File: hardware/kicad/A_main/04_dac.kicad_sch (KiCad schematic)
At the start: 34 parts, among them J30 SMA TX1, J31 SMA TX2, J32 SMA TX3, J33 SMA TX4, T10 ADT1-1WT+, T11 ADT1-1WT+, T12 ADT1-1WT+, T13 ADT1-1WT+, U10 LFE5U-25F-7BG256I, U30 AD9767ASTZ, U31 AD9767ASTZ

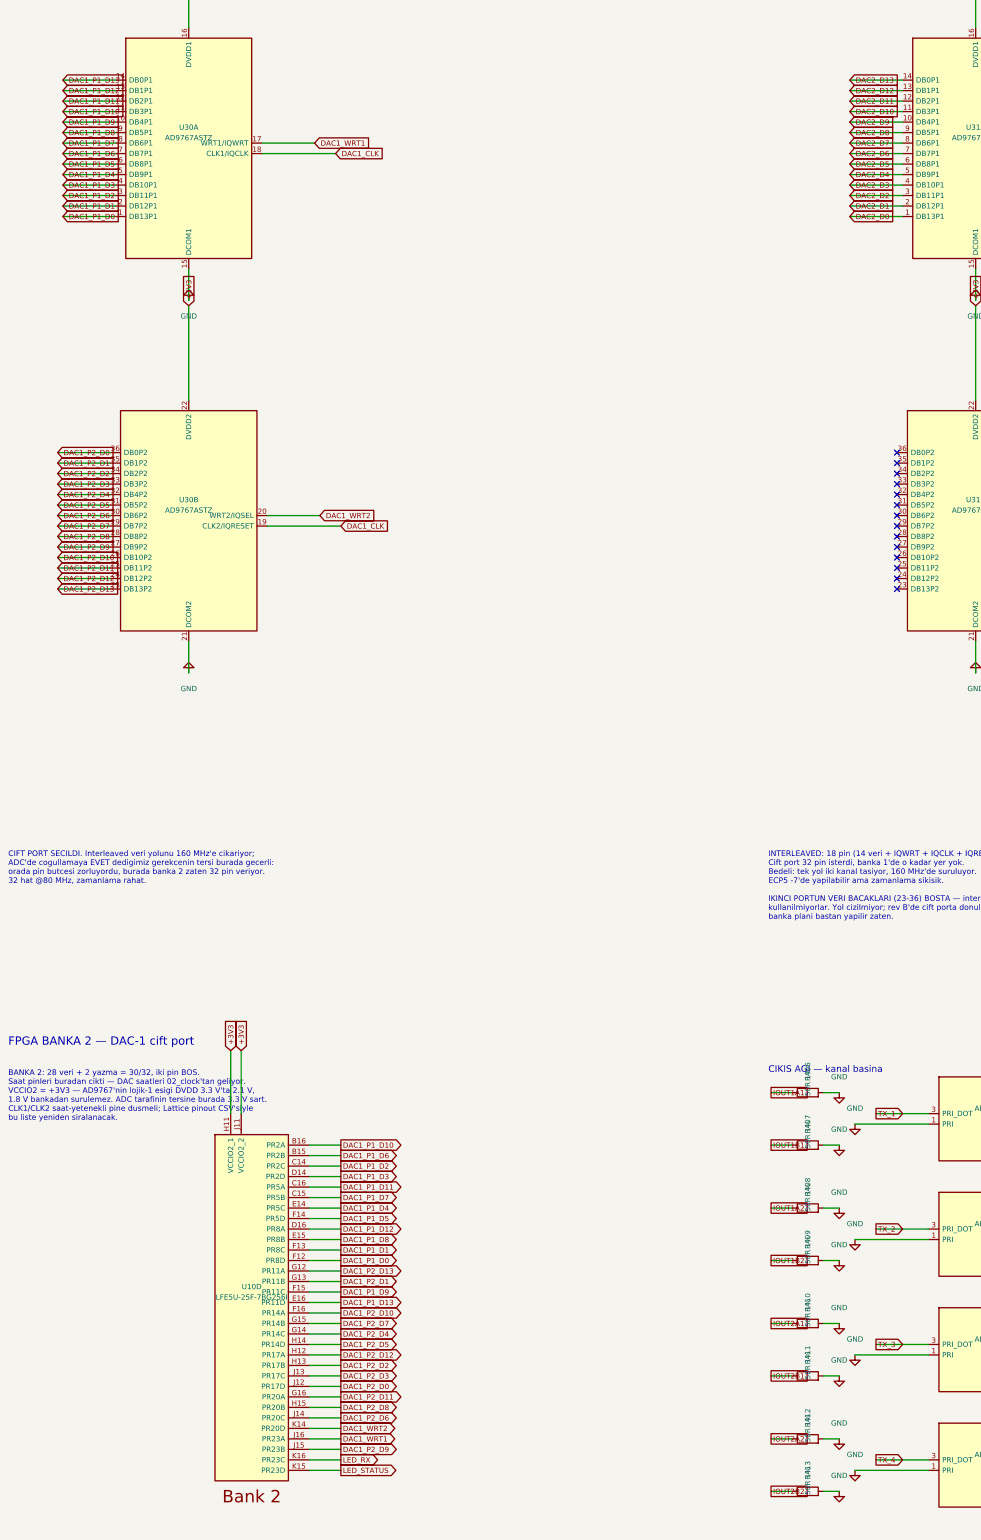
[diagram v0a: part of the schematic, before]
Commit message: Connect the pads that had no net
A symbol pin number must agree with the footprint pad number. If the
numbers do not agree, the net goes nowhere. The netlist removes it
and gives no message. ERC examines the schematic and sees a wire. DRC
does not count an unconnected pad as a violation. All three boards
showed zero ERC violations while 31 pads had no net.

Two of these faults stopped a board.

The footprint of the Ethernet PHY was for a different part. The
project used QFN-48 6x6 mm with 0.4 mm pitch. The RTL8211F(I)-CG is
WQFN-40-EP 5x5 mm. You cannot solder the part to that pad pattern.

The 25 MHz crystal had a 2-pin symbol on a 4-pad footprint. On a 3225
crystal the terminals are the diagonal pads 1 and 3. Pads 2 and 4 are
the metal can. XO went to pad 2. There was no crystal between XI and
XO, and thus neither PHY could make a clock.

The paddle of the AD9251 was pin 0 in the symbol and pad 65 in the
footprint. The paddle of the PE4312 was Pad against pad 21. The gas
discharge tubes had one electrode unconnected, because
Device:GDT_2Pin uses pins 1 and 3 but the varistor footprint uses
pads 1 and 2. A local footprint with pads 1 and 3 corrects this.

ped_denetim.py finds these faults on the board. yap.sh runs it before
the DSN export. The chain stops if a pad has no net.

The DSN export also changed. It declared In1 and In4 as power layers
but did not export the copper on them. The router thus believed that
the two ground planes were empty. It routed the 289 pins of GND as
traces on the signal layers. The planes now go out as conduction
areas.
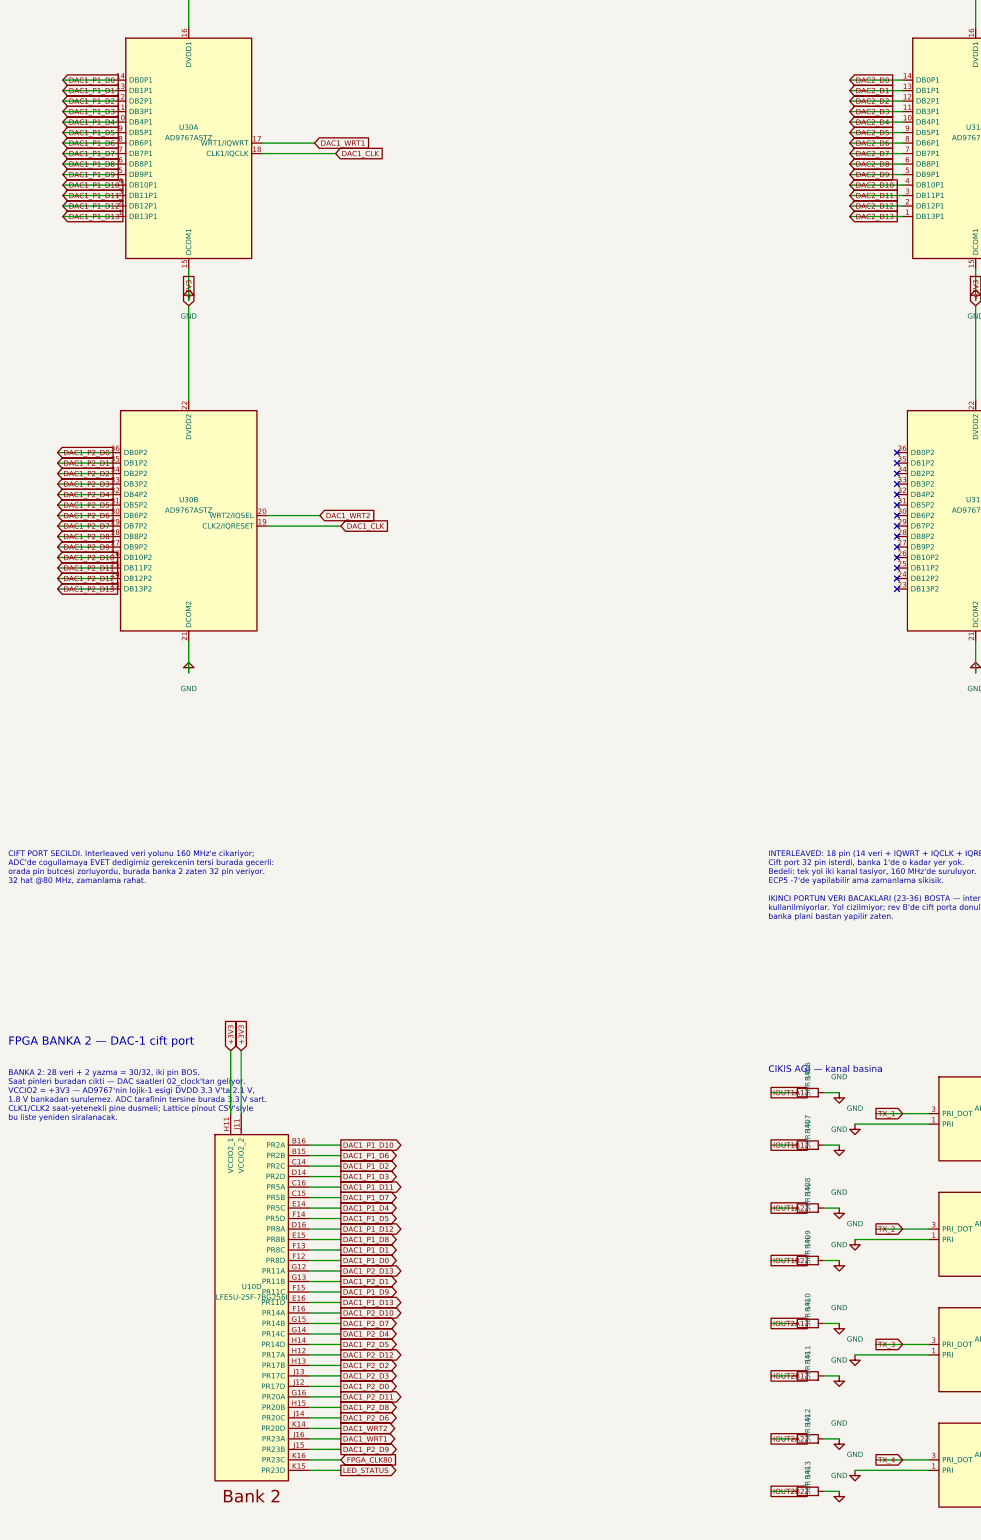
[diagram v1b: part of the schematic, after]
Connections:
- net DAC1_P1_D0: now also U30.14 (DB0P1); no longer U30.1 (DB13P1)
- net DAC1_P1_D1: now also U30.13 (DB1P1); no longer U30.2 (DB12P1)
- net DAC1_P1_D10: now also U30.4 (DB10P1); no longer U30.11 (DB3P1)
- net DAC1_P1_D11: now also U30.3 (DB11P1); no longer U30.12 (DB2P1)
- net DAC1_P1_D12: now also U30.2 (DB12P1); no longer U30.13 (DB1P1)
- net DAC1_P1_D13: now also U30.1 (DB13P1); no longer U30.14 (DB0P1)
- net DAC1_P1_D2: now also U30.12 (DB2P1); no longer U30.3 (DB11P1)
- net DAC1_P1_D3: now also U30.11 (DB3P1); no longer U30.4 (DB10P1)
- net DAC1_P1_D4: now also U30.10 (DB4P1); no longer U30.5 (DB9P1)
- net DAC1_P1_D5: now also U30.9 (DB5P1); no longer U30.6 (DB8P1)
- net DAC1_P1_D6: now also U30.8 (DB6P1); no longer U30.7 (DB7P1)
- net DAC1_P1_D7: now also U30.7 (DB7P1); no longer U30.8 (DB6P1)
- net DAC1_P1_D8: now also U30.6 (DB8P1); no longer U30.9 (DB5P1)
- net DAC1_P1_D9: now also U30.5 (DB9P1); no longer U30.10 (DB4P1)
- net DAC2_D0: now also U31.14 (DB0P1); no longer U31.1 (DB13P1)
- net DAC2_D1: now also U31.13 (DB1P1); no longer U31.2 (DB12P1)
- net DAC2_D10: now also U31.4 (DB10P1); no longer U31.11 (DB3P1)
- net DAC2_D11: now also U31.3 (DB11P1); no longer U31.12 (DB2P1)
- net DAC2_D12: now also U31.2 (DB12P1); no longer U31.13 (DB1P1)
- net DAC2_D13: now also U31.1 (DB13P1); no longer U31.14 (DB0P1)
- net DAC2_D2: now also U31.12 (DB2P1); no longer U31.3 (DB11P1)
- net DAC2_D3: now also U31.11 (DB3P1); no longer U31.4 (DB10P1)
- net DAC2_D4: now also U31.10 (DB4P1); no longer U31.5 (DB9P1)
- net DAC2_D5: now also U31.9 (DB5P1); no longer U31.6 (DB8P1)
- net DAC2_D6: now also U31.8 (DB6P1); no longer U31.7 (DB7P1)
- net DAC2_D7: now also U31.7 (DB7P1); no longer U31.8 (DB6P1)
- net DAC2_D8: now also U31.6 (DB8P1); no longer U31.9 (DB5P1)
- net DAC2_D9: now also U31.5 (DB9P1); no longer U31.10 (DB4P1)
- net LED_RX renamed FPGA_CLK80

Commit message: Correct the clearance test for the pre-routed traces
The clearance test used a circle for each pad. The radius was
max(width, height)/2. The corner of a rectangle is at
hypot(width, height)/2 from the center. The test thus made the pad
smaller than it is. On the 2.5 x 4.5 mm gate pad of a TO-247 the
difference is 2.250 mm against 2.574 mm.

The DRN_A trace was on the gate pad of Q10 with an overlap of 35 um.
This is a short circuit between the 50 V drain rail and the gate of a
100 W device. The search that finds the tee offset accepted this
route. The overlap is at a corner and 35 um wide. You cannot see it
on a plot.

The test now uses the real shape of the pad and the collision test of
pcbnew. It also uses the 300 um clearance and not only an overlap. A
trace that is 50 um from a pad is also not possible to manufacture.

Board D was built again. No trace is below 300 um and the smallest
gap is 0.537 mm. Boards A and C were correct.
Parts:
- removed C400, C403: 100nF, Capacitor_SMD:C_0603_1608Metric, symbol Device:C
- removed C460, C461, C470, C471, C472, C473: 100nF, Capacitor_SMD:C_0402_1005Metric, symbol Device:C
- removed C480, C481: 10uF, Capacitor_SMD:C_0402_1005Metric, symbol Device:C
- removed J30: SMA TX1, Connector_Coaxial:SMA_Amphenol_132289_EdgeMount, symbol Connector:Conn_Coaxial
- removed J31: SMA TX2, Connector_Coaxial:SMA_Amphenol_132289_EdgeMount, symbol Connector:Conn_Coaxial
- removed J32: SMA TX3, Connector_Coaxial:SMA_Amphenol_132289_EdgeMount, symbol Connector:Conn_Coaxial
- removed J33: SMA TX4, Connector_Coaxial:SMA_Amphenol_132289_EdgeMount, symbol Connector:Conn_Coaxial
- removed R401, R402, R404, R405: 1.92k 1%, Resistor_SMD:R_0603_1608Metric, symbol Device:R
- removed R406, R407, R408, R409, R410, R411, R412, R413: 50R 1%, Resistor_SMD:R_0603_1608Metric, symbol Device:R
- removed R450: 0R, Resistor_SMD:R_0603_1608Metric, symbol Device:R
- removed T10, T11, T12, T13: ADT1-1WT+, RF_Mini-Circuits:Mini-Circuits_CD542_H2.84mm, symbol dogrudan-sdr:ADT1-1WT
- removed U10: LFE5U-25F-7BG256I, Package_BGA:BGA-256_14.0x14.0mm_Layout16x16_P0.8mm_Ball0.45mm_Pad0.32mm_NSMD, symbol dogrudan-sdr:ECP5-BGA256
- removed U30, U31: AD9767ASTZ, Package_QFP:LQFP-48_7x7mm_P0.5mm, symbol dogrudan-sdr:AD9767
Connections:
- no-connect marks 18 -> 0
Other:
- note added: "DAC x2 AD9767 x2, cift port + interleaved, banka 2/1 Baglantilar: ../NETLIST.md"
- note removed: "ANALOG CIKIS VE REFERANS — birim 3"
- note removed: "AVDD (47) her cipte 1, DVDD1/DVDD2 (16, 22) her cipte 2. AVDD +3V3_A'dan (kendi LDO'su), DVDD ana +3V3'ten — DAC'in dijital anahtarlamasi analog tarafa kuplemasin."
- note removed: "AYRISTIRMA"
- note removed: "BANKA 2: 28 veri + 2 yazma = 30/32, iki pin BOS. Saat pinleri buradan cikti — DAC saatleri 02_clock'tan geliyor. VCCIO2 = +3V3 — AD9767'nin lojik-1 esigi DVDD 3.3 V'ta 2.1 V, 1.8 V bankadan surulemez. ADC tarafinin tersine burada 3.3 V sart. CLK1/CLK2 saat-yetenekli pine dusmeli; Lattice pinout CSV'siyle bu liste yeniden siralanacak."
- note removed: "CIFT PORT SECILDI. Interleaved veri yolunu 160 MHz'e cikariyor; ADC'de cogullamaya EVET dedigimiz gerekcenin tersi burada gecerli: orada pin butcesi zorluyordu, burada banka 2 zaten 32 pin veriyor. 32 hat @80 MHz, zamanlama rahat."
- note removed: "CIKIS AGI — kanal basina"
- note removed: "DAC-1 — CIFT PORT (MODE = HIGH), banka 2"
- note removed: "DAC-2 MODE bacagi 0R ile toprakta. Dogrudan bakir yerine direnc: cift porta donme karari cikarsa direnci +3V3'e almak yetiyor, kart kesilmiyor."
- note removed: "DAC-2 — INTERLEAVED (MODE = LOW), banka 1"
- note removed: "FPGA BANKA 2 — DAC-1 cift port"
- note removed: "INTERLEAVED: 18 pin (14 veri + IQWRT + IQCLK + IQRESET + IQSEL). Cift port 32 pin isterdi, banka 1'de o kadar yer yok. Bedeli: tek yol iki kanal tasiyor, 160 MHz'de suruluyor. ECP5 -7'de yapilabilir ama zamanlama sikisik. IKINCI PORTUN VERI BACAKLARI (23-36) BOSTA — interleaved modda kullanilmiyorlar. Yol cizilmiyor; rev B'de cift porta donulurse banka plani bastan yapilir zaten."
- note removed: "IOUTFS = 32 x (1.2 / R_set). 20 mA icin R_set = 1.92k. %1 direnc: %5 kullanilirsa cikis genligi %5 kayiyor ve iki DAC arasinda dengesizlik olusuyor — MIMO'da genlik esitligi lazim. GAINCTRL ACOM'da = dahili 1.2 V referans, master modu. REFIO 100nF ile ACOM'a."
- note removed: "Rekonstruksiyon filtresi (36 MHz LPF) ve surucu C KARTINDA. Burada sadece 50R cift sonlandirma + trafo kuplaj var — datasheet onerdigi cikis agi. Filtre bant secimine bagli, o yuzden ayri kartta; TX bandi degistirilirse burasi degismiyor."

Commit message: Correct the schematic faults that ERC cannot find
An agent examined the three schematics against the datasheets. ERC
reported zero violations before and after this work. None of these
faults are visible to ERC.

The comparator for the external 10 MHz reference was in shutdown. The
SHDN pin of the TLV3501 went to +3V3. Sixteen DRV8833 devices had VCP
and VINT unconnected. Without the charge pump none of the 28 filter
relays can latch. Seven regulators had no decoupling capacitor within
18 mm to 94 mm. On board D the nearest +12V capacitor to an LM358 was
227 mm away on a 275 mm board.

The PE4312 devices had no series 10k resistor on pin 3. The datasheet
makes this necessary for the attenuation accuracy. Their exposed pad
was 2.6 mm against 2.15 mm. The BOM did not give the load capacitance
of the crystal. This work added 60 parts and changed 4 footprints.

The worst fault was in the tool chain. lib/gen_symbols.py still made
the old pin numbers. The five corrections went into the symbol
library by hand and not into its generator. A new library would have
removed all of them.

The thermal vias are now a decision from the measured clearance and
the dissipation. This work removed them from the PE4312, the RTL8211F
and the ADCLK846. They stay on the DRV8833 and on the LM5164, which
is a 1 W buck converter.

Two checks are new. sema_denetim compares the pin names with the
nets. netlist_denetim locks 22 pin-to-net expectations from the
datasheets and does not need a board.

The boards were built again with these corrections. The chain now
adds the test points: 10 on board A, 7 on board C and 15 on board D.
Each board has 3 fiducials. Every pad has a net.
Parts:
- added C400, C403: 100nF, Capacitor_SMD:C_0603_1608Metric, symbol Device:C
- added C460, C461, C470, C471, C472, C473: 100nF, Capacitor_SMD:C_0402_1005Metric, symbol Device:C
- added C480, C481: 10uF, Capacitor_SMD:C_0402_1005Metric, symbol Device:C
- added J30: SMA TX1, Connector_Coaxial:SMA_Amphenol_132289_EdgeMount, symbol Connector:Conn_Coaxial
- added J31: SMA TX2, Connector_Coaxial:SMA_Amphenol_132289_EdgeMount, symbol Connector:Conn_Coaxial
- added J32: SMA TX3, Connector_Coaxial:SMA_Amphenol_132289_EdgeMount, symbol Connector:Conn_Coaxial
- added J33: SMA TX4, Connector_Coaxial:SMA_Amphenol_132289_EdgeMount, symbol Connector:Conn_Coaxial
- added R401, R402, R404, R405: 1.92k 1%, Resistor_SMD:R_0603_1608Metric, symbol Device:R
- added R406, R407, R408, R409, R410, R411, R412, R413: 50R 1%, Resistor_SMD:R_0603_1608Metric, symbol Device:R
- added R450: 0R, Resistor_SMD:R_0603_1608Metric, symbol Device:R
- added T10, T11, T12, T13: ADT1-1WT+, RF_Mini-Circuits:Mini-Circuits_CD542_H2.84mm, symbol dogrudan-sdr:ADT1-1WT
- added U10: LFE5U-25F-7BG256I, Package_BGA:BGA-256_14.0x14.0mm_Layout16x16_P0.8mm_Ball0.45mm_Pad0.32mm_NSMD, symbol dogrudan-sdr:ECP5-BGA256
- added U30, U31: AD9767ASTZ, Package_QFP:LQFP-48_7x7mm_P0.5mm, symbol dogrudan-sdr:AD9767
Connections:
- new net +3V3: C470.1, C471.1, C472.1, C473.1, U10.H11 (VCCIO2_1), U10.J11 (VCCIO2_2), U30.16 (DVDD1), U30.22 (DVDD2), U30.48 (MODE), U31.16 (DVDD1), U31.22 (DVDD2)
- new net +3V3_A: C460.1, C461.1, C480.1, C481.1, U30.47 (AVDD), U31.47 (AVDD)
- new net DAC1_CLK: U30.18 (CLK1/IQCLK), U30.19 (CLK2/IQRESET)
- new net DAC1_P1_D0: U10.F12 (PR8D), U30.14 (DB0P1)
- new net DAC1_P1_D1: U10.F13 (PR8C), U30.13 (DB1P1)
- new net DAC1_P1_D10: U10.B16 (PR2A), U30.4 (DB10P1)
- new net DAC1_P1_D11: U10.C16 (PR5A), U30.3 (DB11P1)
- new net DAC1_P1_D12: U10.D16 (PR8A), U30.2 (DB12P1)
- new net DAC1_P1_D13: U10.E16 (PR11D), U30.1 (DB13P1)
- new net DAC1_P1_D2: U10.C14 (PR2C), U30.12 (DB2P1)
- new net DAC1_P1_D3: U10.D14 (PR2D), U30.11 (DB3P1)
- new net DAC1_P1_D4: U10.E14 (PR5C), U30.10 (DB4P1)
- new net DAC1_P1_D5: U10.F14 (PR5D), U30.9 (DB5P1)
- new net DAC1_P1_D6: U10.B15 (PR2B), U30.8 (DB6P1)
- new net DAC1_P1_D7: U10.C15 (PR5B), U30.7 (DB7P1)
- new net DAC1_P1_D8: U10.E15 (PR8B), U30.6 (DB8P1)
- new net DAC1_P1_D9: U10.F15 (PR11C), U30.5 (DB9P1)
- new net DAC1_P2_D0: U10.J12 (PR17D), U30.36 (DB0P2)
- new net DAC1_P2_D1: U10.G13 (PR11B), U30.35 (DB1P2)
- new net DAC1_P2_D10: U10.F16 (PR14A), U30.26 (DB10P2)
- new net DAC1_P2_D11: U10.G16 (PR20A), U30.25 (DB11P2)
- new net DAC1_P2_D12: U10.H12 (PR17A), U30.24 (DB12P2)
- new net DAC1_P2_D13: U10.G12 (PR11A), U30.23 (DB13P2)
- new net DAC1_P2_D2: U10.H13 (PR17B), U30.34 (DB2P2)
- new net DAC1_P2_D3: U10.J13 (PR17C), U30.33 (DB3P2)
- new net DAC1_P2_D4: U10.G14 (PR14C), U30.32 (DB4P2)
- new net DAC1_P2_D5: U10.H14 (PR14D), U30.31 (DB5P2)
- new net DAC1_P2_D6: U10.J14 (PR20C), U30.30 (DB6P2)
- new net DAC1_P2_D7: U10.G15 (PR14B), U30.29 (DB7P2)
- new net DAC1_P2_D8: U10.H15 (PR20B), U30.28 (DB8P2)
- new net DAC1_P2_D9: U10.J15 (PR23B), U30.27 (DB9P2)
- new net DAC1_WRT1: U10.J16 (PR23A), U30.17 (WRT1/IQWRT)
- new net DAC1_WRT2: U10.K14 (PR20D), U30.20 (WRT2/IQSEL)
- new net DAC2_CLK: U31.18 (CLK1/IQCLK)
- new net DAC2_D0: U31.14 (DB0P1)
- new net DAC2_D1: U31.13 (DB1P1)
- new net DAC2_D10: U31.4 (DB10P1)
- new net DAC2_D11: U31.3 (DB11P1)
- new net DAC2_D12: U31.2 (DB12P1)
- new net DAC2_D13: U31.1 (DB13P1)
- new net DAC2_D2: U31.12 (DB2P1)
- new net DAC2_D3: U31.11 (DB3P1)
- new net DAC2_D4: U31.10 (DB4P1)
- new net DAC2_D5: U31.9 (DB5P1)
- new net DAC2_D6: U31.8 (DB6P1)
- new net DAC2_D7: U31.7 (DB7P1)
- new net DAC2_D8: U31.6 (DB8P1)
- new net DAC2_D9: U31.5 (DB9P1)
- new net DAC2_IQRESET: U31.19 (CLK2/IQRESET)
- new net DAC2_IQSEL: U31.20 (WRT2/IQSEL)
- new net DAC2_IQWRT: U31.17 (WRT1/IQWRT)
- new net FPGA_CLK80: U10.K16 (PR23C)
- new net FSADJ1_U30: R401.1, U30.44 (FSADJ1)
- new net FSADJ1_U31: R404.1, U31.44 (FSADJ1)
- new net FSADJ2_U30: R402.1, U30.41 (FSADJ2)
- new net FSADJ2_U31: R405.1, U31.41 (FSADJ2)
- new net GND: C400.2, C403.2, C460.2, C461.2, C470.2, C471.2, C472.2, C473.2, C480.2, C481.2, J30.2 (Ext), J31.2 (Ext), J32.2 (Ext), J33.2 (Ext), R401.2, R402.2, R404.2, R405.2, R406.2, R407.2, R408.2, R409.2, R410.2, R411.2, R412.2, R413.2, R450.2, T10.1 (PRI), T10.2 (SEC_CT), T11.1 (PRI), T11.2 (SEC_CT), T12.1 (PRI), T12.2 (SEC_CT), T13.1 (PRI), T13.2 (SEC_CT), U30.15 (DCOM1), U30.21 (DCOM2), U30.37 (SLEEP), U30.38 (ACOM), U30.42 (GAINCTRL), U31.15 (DCOM1), U31.21 (DCOM2), U31.37 (SLEEP), U31.38 (ACOM), U31.42 (GAINCTRL)
- new net GND_MODE: R450.1, U31.48 (MODE)
- new net IOUT1A1: R406.1, T10.6 (SEC_DOT), U30.46 (IOUTA1)
- new net IOUT1A2: R408.1, T11.6 (SEC_DOT), U30.39 (IOUTA2)
- new net IOUT1B1: R407.1, T10.4 (SEC), U30.45 (IOUTB1)
- new net IOUT1B2: R409.1, T11.4 (SEC), U30.40 (IOUTB2)
- new net IOUT2A1: R410.1, T12.6 (SEC_DOT), U31.46 (IOUTA1)
- new net IOUT2A2: R412.1, T13.6 (SEC_DOT), U31.39 (IOUTA2)
- new net IOUT2B1: R411.1, T12.4 (SEC), U31.45 (IOUTB1)
- new net IOUT2B2: R413.1, T13.4 (SEC), U31.40 (IOUTB2)
- new net LED_STATUS: U10.K15 (PR23D)
- new net REFIO_U30: C400.1, U30.43 (REFIO)
- new net REFIO_U31: C403.1, U31.43 (REFIO)
- new net TX_1: J30.1 (In), T10.3 (PRI_DOT)
- new net TX_2: J31.1 (In), T11.3 (PRI_DOT)
- new net TX_3: J32.1 (In), T12.3 (PRI_DOT)
- new net TX_4: J33.1 (In), T13.3 (PRI_DOT)
- no-connect marks 0 -> 18
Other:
- note added: "ANALOG CIKIS VE REFERANS — birim 3"
- note added: "AVDD (47) her cipte 1, DVDD1/DVDD2 (16, 22) her cipte 2. AVDD +3V3_A'dan (kendi LDO'su), DVDD ana +3V3'ten — DAC'in dijital anahtarlamasi analog tarafa kuplemasin."
- note added: "AYRISTIRMA"
- note added: "BANKA 2: 28 veri + 2 yazma = 30/32, iki pin BOS. Saat pinleri buradan cikti — DAC saatleri 02_clock'tan geliyor. VCCIO2 = +3V3 — AD9767'nin lojik-1 esigi DVDD 3.3 V'ta 2.1 V, 1.8 V bankadan surulemez. ADC tarafinin tersine burada 3.3 V sart. CLK1/CLK2 saat-yetenekli pine dusmeli; Lattice pinout CSV'siyle bu liste yeniden siralanacak."
- note added: "CIFT PORT SECILDI. Interleaved veri yolunu 160 MHz'e cikariyor; ADC'de cogullamaya EVET dedigimiz gerekcenin tersi burada gecerli: orada pin butcesi zorluyordu, burada banka 2 zaten 32 pin veriyor. 32 hat @80 MHz, zamanlama rahat."
- note added: "CIKIS AGI — kanal basina"
- note added: "DAC-1 — CIFT PORT (MODE = HIGH), banka 2"
- note added: "DAC-2 MODE bacagi 0R ile toprakta. Dogrudan bakir yerine direnc: cift porta donme karari cikarsa direnci +3V3'e almak yetiyor, kart kesilmiyor."
- note added: "DAC-2 — INTERLEAVED (MODE = LOW), banka 1"
- note added: "FPGA BANKA 2 — DAC-1 cift port"
- note added: "INTERLEAVED: 18 pin (14 veri + IQWRT + IQCLK + IQRESET + IQSEL). Cift port 32 pin isterdi, banka 1'de o kadar yer yok. Bedeli: tek yol iki kanal tasiyor, 160 MHz'de suruluyor. ECP5 -7'de yapilabilir ama zamanlama sikisik. IKINCI PORTUN VERI BACAKLARI (23-36) BOSTA — interleaved modda kullanilmiyorlar. Yol cizilmiyor; rev B'de cift porta donulurse banka plani bastan yapilir zaten."
- note added: "IOUTFS = 32 x (1.2 / R_set). 20 mA icin R_set = 1.92k. %1 direnc: %5 kullanilirsa cikis genligi %5 kayiyor ve iki DAC arasinda dengesizlik olusuyor — MIMO'da genlik esitligi lazim. GAINCTRL ACOM'da = dahili 1.2 V referans, master modu. REFIO 100nF ile ACOM'a."
- note added: "Rekonstruksiyon filtresi (36 MHz LPF) ve surucu C KARTINDA. Burada sadece 50R cift sonlandirma + trafo kuplaj var — datasheet onerdigi cikis agi. Filtre bant secimine bagli, o yuzden ayri kartta; TX bandi degistirilirse burasi degismiyor."
- note removed: "DAC x2 AD9767 x2, cift port + interleaved, banka 2/1 Baglantilar: ../NETLIST.md"
